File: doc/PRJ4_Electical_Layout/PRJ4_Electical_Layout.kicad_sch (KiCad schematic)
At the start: 10 parts, among them M1 Motor_DC, M2 Motor_DC, U5 MCP23017_SO

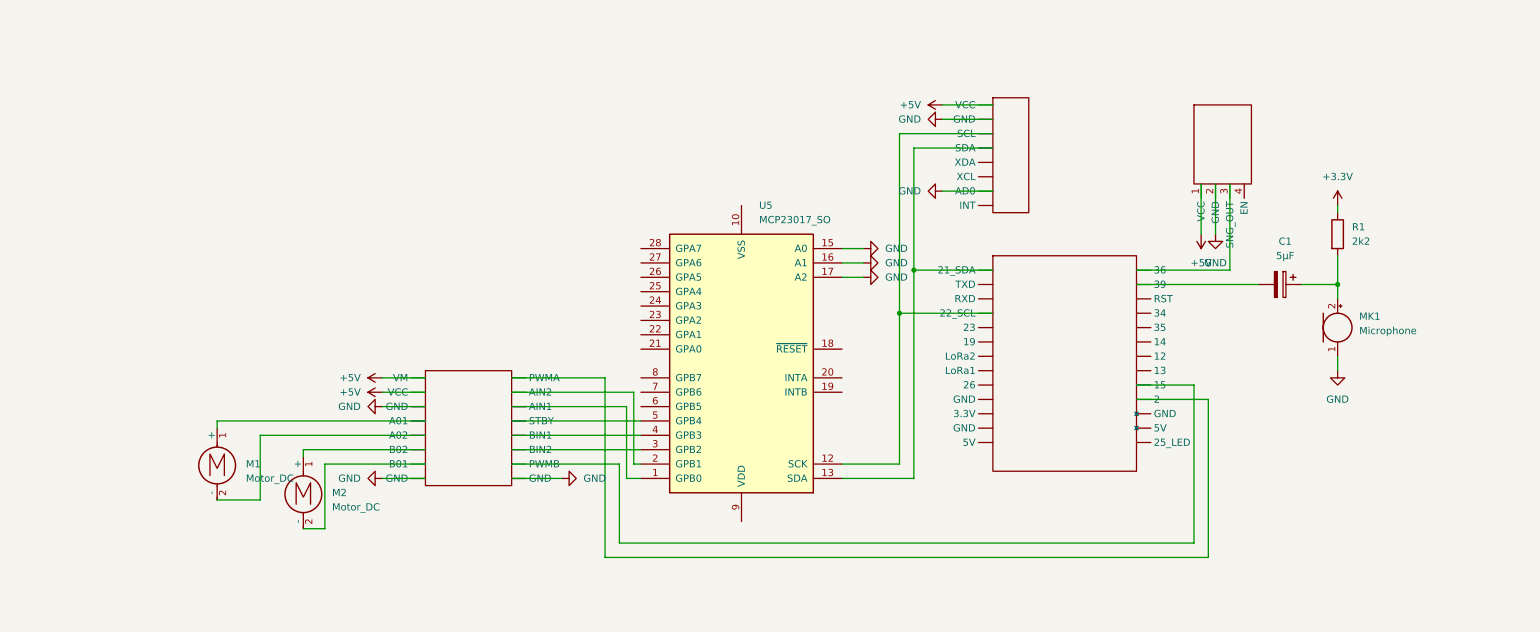
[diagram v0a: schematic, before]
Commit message: Add new components
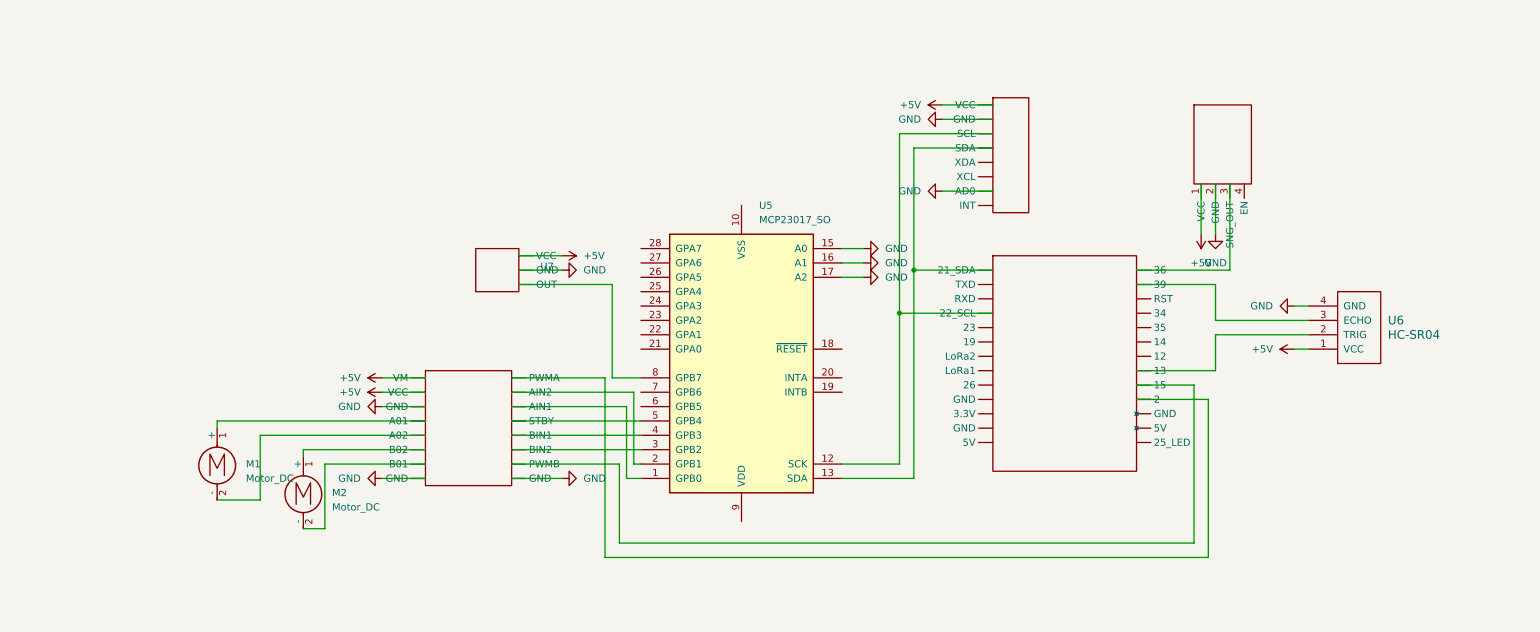
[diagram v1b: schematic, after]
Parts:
- removed C1: 5µF, symbol Device:C_Polarized
- removed MK1: Microphone, symbol Device:Microphone
- removed R1: 2k2, symbol Device:R
- added U6: HC-SR04, symbol hc-sr04:HC-SR04
- added U7: ~, symbol prj4:MAX4466
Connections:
- net +5V: now also U6.1 (VCC), U7. (VCC)
- net GND: now also U6.4 (GND), U7. (VCC)
- net at U2. (25_LED): now also U6.3 (ECHO)
- net at U5.8 (GPB7): now also U7. (VCC)
- new net: U2. (25_LED), U3. (INT), U5.12 (SCK)
- new net: U2. (25_LED), U3. (INT), U5.13 (SDA)
- new net: U2. (25_LED), U4. (GND) (x2)
- new net: U2. (25_LED), U6.2 (TRIG)

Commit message: Update layout with new 2. mic
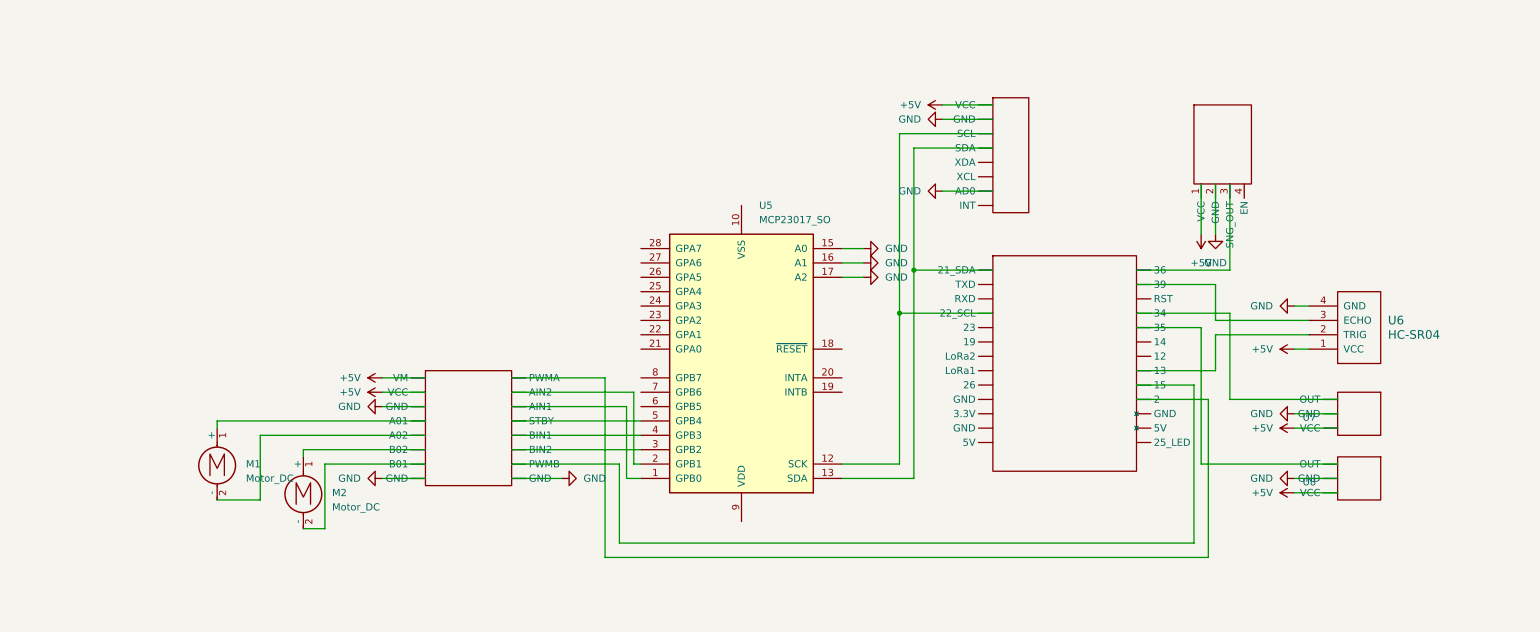
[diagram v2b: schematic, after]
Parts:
- added U8: ~, symbol prj4:MAX4466
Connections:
- net +5V: now also U8. (VCC)
- net GND: now also U8. (VCC)
- net at U2. (25_LED): now also U6.3 (ECHO)
- net at U5.8 (GPB7): no longer U7. (VCC)
- new net: U2. (25_LED), U3. (INT), U5.12 (SCK)
- new net: U2. (25_LED), U3. (INT), U5.13 (SDA)
- new net: U2. (25_LED), U7. (VCC)
- new net: U2. (25_LED), U8. (VCC)
- new net: U2. (25_LED), U4. (GND) (x2)
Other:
- moved on the sheet: U7

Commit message: add new components plus change esp 32
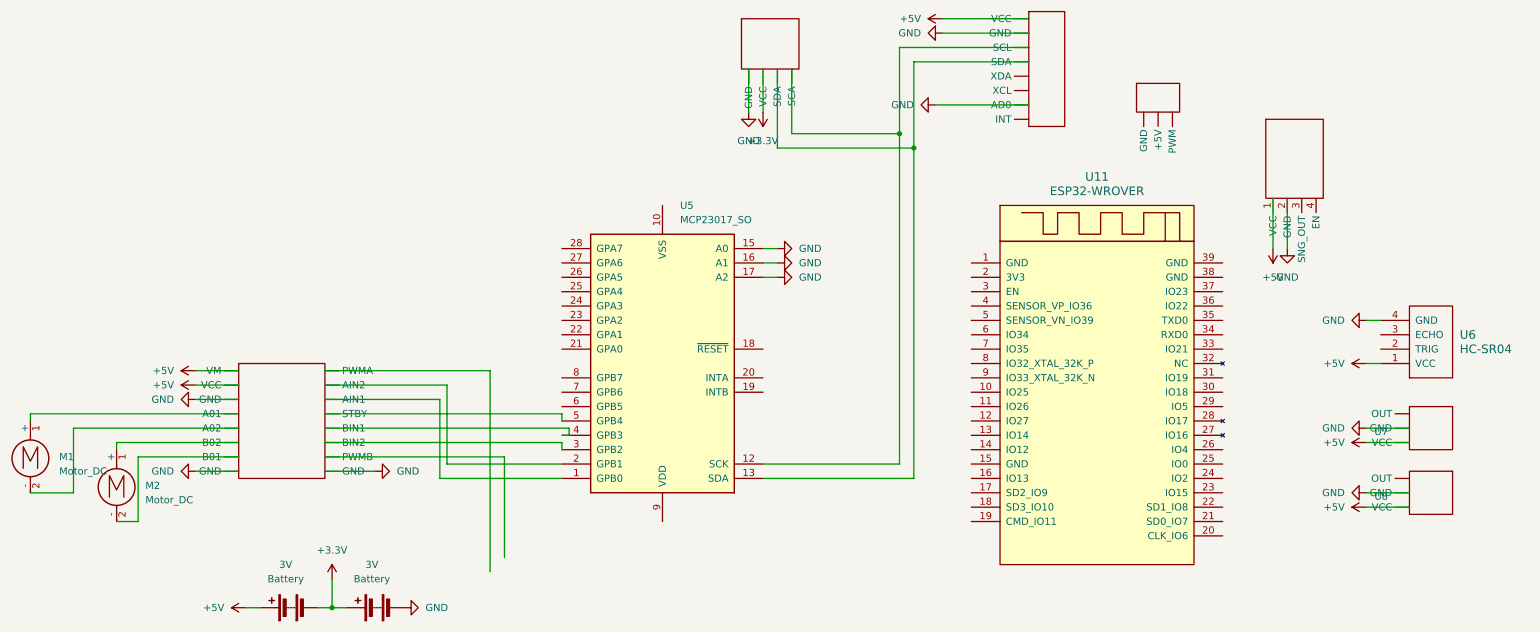
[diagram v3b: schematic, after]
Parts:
- removed U2: ~, symbol prj4:lilygo_t3
- added 3V (x2): Battery, symbol Device:Battery
- added U10: ~, symbol prj4:996_Servo
- added U11: ESP32-WROVER, symbol esp32-wrover:ESP32-WROVER
- added U9: ~, symbol prj4:Monitor
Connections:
- net +5V: now also 3V.1 (+)
- net GND: now also 3V.2 (-), U9. (SCA)
- net at U3. (INT), U5.12 (SCK): now also U9. (SCA)
- net at U3. (INT), U5.13 (SDA): now also U9. (SCA)
- new net +3.3V: 3V.1 (+), 3V.2 (-), U9. (SCA)
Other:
- moved on the sheet: M1, M2, U5, U6, U7, U8

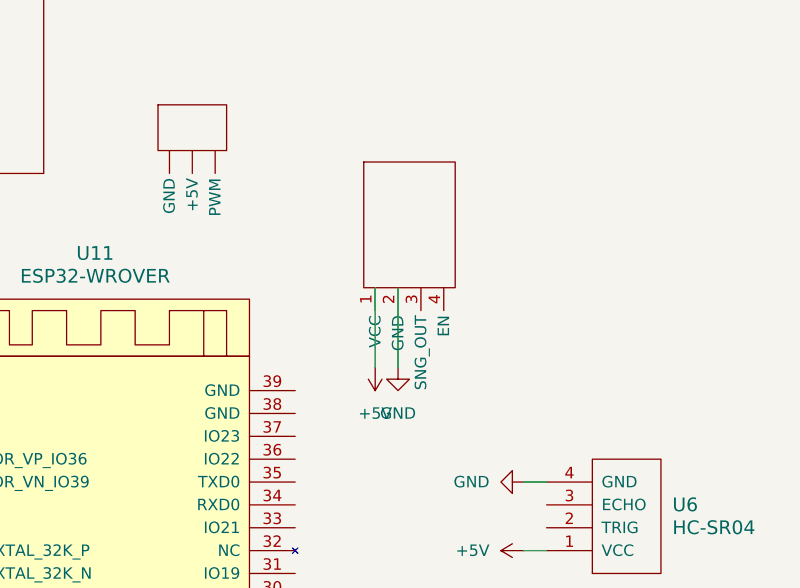
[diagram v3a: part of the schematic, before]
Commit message: remove ir sensor
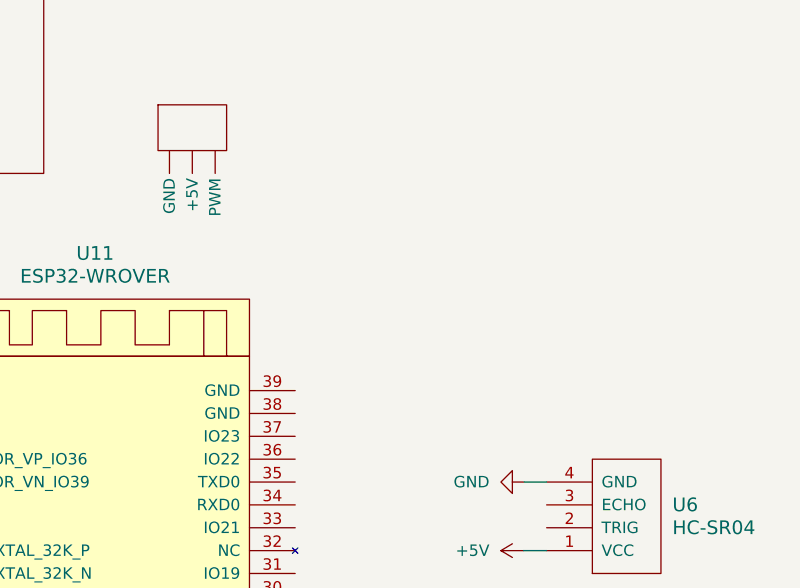
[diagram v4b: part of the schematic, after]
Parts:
- removed U1: ~, symbol prj4:SEN-KY032IR
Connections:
- new net: U3. (INT), U5.12 (SCK), U9. (SCA)
- new net: U3. (INT), U5.13 (SDA), U9. (SCA)
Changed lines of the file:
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@@
 	(wire
 		(pts
-			(xy 243.84 57.15) (xy 243.84 66.04)
+			(xy 50.8 105.41) (xy 58.42 105.41)
 		)
 		(stroke
@@
 	(wire
 		(pts
-			(xy 50.8 105.41) (xy 58.42 105.41)
+			(xy 21.59 95.25) (xy 21.59 96.52)
 		)
 		(stroke
@@
 	(wire
 		(pts
-			(xy 21.59 95.25) (xy 21.59 96.52)
+			(xy 151.13 66.04) (xy 153.67 66.04)
 		)
 		(stroke
@@
 	(wire
 		(pts
-			(xy 151.13 66.04) (xy 153.67 66.04)
+			(xy 151.13 104.14) (xy 175.26 104.14)
 		)
 		(stroke
@@
 	(wire
 		(pts
-			(xy 151.13 104.14) (xy 175.26 104.14)
+			(xy 58.42 100.33) (xy 36.83 100.33)
 		)
 		(stroke
@@
 	(wire
 		(pts
-			(xy 58.42 100.33) (xy 36.83 100.33)
+			(xy 177.8 33.02) (xy 198.12 33.02)
 		)
 		(stroke
@@
 	(wire
 		(pts
-			(xy 177.8 33.02) (xy 198.12 33.02)
+			(xy 29.21 109.22) (xy 21.59 109.22)
 		)
 		(stroke
@@
 	(wire
 		(pts
-			(xy 29.21 109.22) (xy 21.59 109.22)
+			(xy 74.93 124.46) (xy 74.93 129.54)
 		)
 		(stroke
@@
 	(wire
 		(pts
-			(xy 74.93 124.46) (xy 74.93 129.54)
+			(xy 74.93 129.54) (xy 77.47 129.54)
 		)
 		(stroke
@@
 	(wire
 		(pts
-			(xy 74.93 129.54) (xy 77.47 129.54)
+			(xy 73.66 90.17) (xy 95.25 90.17)
 		)
 		(stroke
@@
 	(wire
 		(pts
-			(xy 73.66 90.17) (xy 95.25 90.17)
+			(xy 148.59 34.29) (xy 148.59 41.91)
 		)
 		(stroke
@@
 	(wire
 		(pts
-			(xy 148.59 34.29) (xy 148.59 41.91)
+			(xy 50.8 90.17) (xy 58.42 90.17)
 		)
 		(stroke
@@
 	(wire
 		(pts
-			(xy 50.8 90.17) (xy 58.42 90.17)
+			(xy 177.8 33.02) (xy 177.8 48.26)
 		)
 		(stroke
@@
 	(wire
 		(pts
-			(xy 177.8 33.02) (xy 177.8 48.26)
+			(xy 177.8 48.26) (xy 177.8 106.68)
 		)
 		(stroke
@@
 	(wire
 		(pts
-			(xy 177.8 48.26) (xy 177.8 106.68)
+			(xy 198.12 30.48) (xy 175.26 30.48)
 		)
 		(stroke
@@
 	(wire
 		(pts
-			(xy 198.12 30.48) (xy 175.26 30.48)
+			(xy 156.21 45.72) (xy 175.26 45.72)
 		)
 		(stroke
@@
 	(wire
 		(pts
-			(xy 156.21 45.72) (xy 175.26 45.72)
+			(xy 93.98 106.68) (xy 115.57 106.68)
 		)
 		(stroke
@@
 	(wire
 		(pts
-			(xy 241.3 57.15) (xy 241.3 66.04)
+			(xy 73.66 87.63) (xy 102.87 87.63)
 		)
 		(stroke
@@
 	(wire
 		(pts
-			(xy 93.98 106.68) (xy 115.57 106.68)
+			(xy 156.21 34.29) (xy 156.21 45.72)
 		)
 		(stroke
@@
 	(wire
 		(pts
-			(xy 73.66 87.63) (xy 102.87 87.63)
+			(xy 58.42 97.79) (xy 29.21 97.79)
 		)
 		(stroke
@@
 		)
 	)
-	(wire
-		(pts
-			(xy 156.21 34.29) (xy 156.21 45.72)
-		)
-		(stroke
-			(width 0)
-			(type default)
-		)
-	)
-	(wire
-		(pts
-			(xy 58.42 97.79) (xy 29.21 97.79)
-		)
-		(stroke
-			(width 0)
-			(type default)
-		)
-	)
 	(symbol
 		(lib_id "power:+5V")
@@
 				(path "/cdbfb8fb-cebf-44e8-ba3a-bda7c53d363b"
 					(reference "#PWR019")
-					(unit 1)
-				)
-			)
-		)
-	)
-	(symbol
-		(lib_id "prj4:SEN-KY032IR")
-		(at 245.11 49.53 0)
-		(unit 1)
-		(exclude_from_sim no)
-		(in_bom yes)
-		(on_board yes)
-		(dnp no)
-		(fields_autoplaced yes)
-		(property "Reference" "U1"
-			(at 245.11 49.53 0)
-			(effects
-				(font
-					(size 1.27 1.27)
-				)
-				(hide yes)
-			)
-		)
-		(property "Value" "~"
-			(at 251.46 51.435 0)
-			(effects
-				(font
-					(size 1.27 1.27)
-				)
-				(justify left)
-			)
-		)
-		(property "Footprint" ""
-			(at 245.11 49.53 0)
-			(effects
-				(font
-					(size 1.27 1.27)
-				)
-				(hide yes)
-			)
-		)
-		(property "Datasheet" ""
-			(at 245.11 49.53 0)
-			(effects
-				(font
-					(size 1.27 1.27)
-				)
-				(hide yes)
-			)
-		)
-		(property "Description" ""
-			(at 245.11 49.53 0)
-			(effects
-				(font
-					(size 1.27 1.27)
-				)
-				(hide yes)
-			)
-		)
-		(pin "3"
-		)
-		(pin "2"
-		)
-		(pin "4"
-		)
-		(pin "1"
-		)
-		(instances
-			(project ""
-				(path "/cdbfb8fb-cebf-44e8-ba3a-bda7c53d363b"
-					(reference "U1")
 					(unit 1)
 				)
@@
 	)
 	(symbol
-		(lib_id "power:+5V")
-		(at 241.3 66.04 180)
-		(unit 1)
-		(exclude_from_sim no)
-		(in_bom yes)
-		(on_board yes)
-		(dnp no)
-		(fields_autoplaced yes)
-		(property "Reference" "#PWR01"
-			(at 241.3 62.23 0)
-			(effects
-				(font
-					(size 1.27 1.27)
-				)
-				(hide yes)
-			)
-		)
-		(property "Value" "+5V"
-			(at 241.3 71.12 0)
-			(effects
-				(font
-					(size 1.27 1.27)
-				)
-			)
-		)
-		(property "Footprint" ""
-			(at 241.3 66.04 0)
-			(effects
-				(font
-					(size 1.27 1.27)
-				)
-				(hide yes)
-			)
-		)
-		(property "Datasheet" ""
-			(at 241.3 66.04 0)
-			(effects
-				(font
-					(size 1.27 1.27)
-				)
-				(hide yes)
-			)
-		)
-		(property "Description" "Power symbol creates a global label with name \"+5V\""
-			(at 241.3 66.04 0)
-			(effects
-				(font
-					(size 1.27 1.27)
-				)
-				(hide yes)
-			)
-		)
-		(pin "1"
-		)
-		(instances
-			(project ""
-				(path "/cdbfb8fb-cebf-44e8-ba3a-bda7c53d363b"
-					(reference "#PWR01")
-					(unit 1)
-				)
-			)
-		)
-	)
-	(symbol
 		(lib_id "power:GND")
 		(at 257.81 97.79 270)
@@
 					(unit 1)
 				)
-			)
-		)
-	)
-	(symbol
-		(lib_id "power:GND")
-		(at 243.84 66.04 0)
-		(unit 1)
-		(exclude_from_sim no)
-		(in_bom yes)
-		(on_board yes)
-		(dnp no)
-		(fields_autoplaced yes)
-		(property "Reference" "#PWR02"
-			(at 243.84 72.39 0)
-			(effects
-				(font
-					(size 1.27 1.27)
-				)
-				(hide yes)
-			)
-		)
-		(property "Value" "GND"
-			(at 243.84 71.12 0)
-			(effects
-				(font
-					(size 1.27 1.27)
-				)
-			)
-		)
-		(property "Footprint" ""
-			(at 243.84 66.04 0)
-			(effects
-				(font
-					(size 1.27 1.27)
-				)
-				(hide yes)
-			)
-		)
-		(property "Datasheet" ""
-			(at 243.84 66.04 0)
-			(effects
-				(font
-					(size 1.27 1.27)
-				)
-				(hide yes)
-			)
-		)
-		(property "Description" "Power symbol creates a global label with name \"GND\" , ground"
-			(at 243.84 66.04 0)
-			(effects
-				(font
-					(size 1.27 1.27)
-				)
-				(hide yes)
-			)
-		)
-		(pin "1"
-		)
-		(instances
-			(project ""
-				(path "/cdbfb8fb-cebf-44e8-ba3a-bda7c53d363b"
-					(reference "#PWR02")
-					(unit 1)
-				)

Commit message: fix lable
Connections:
- net +3.3V: no longer 3V.1 (+), 3V.2 (-)
- net +5V: no longer 3V.1 (+)
- net at U11.20 (CLK_IO6): now also U11.21 (SD0_IO7), U3. (INT), U5.13 (SDA), U9. (SCA)
- net at U11.22 (SD1_IO8): now also U3. (INT), U5.12 (SCK), U9. (SCA)
- net at U11.23 (IO15): now also U8. (VCC)
- net at U11.24 (IO2): now also U4. (GND)
- net at U11.26 (IO4): now also U7. (VCC)
- net at U11.29 (IO5): now also U4. (GND)
- net at U11.30 (IO18): now also U6.2 (TRIG)
- net at U11.31 (IO19): now also U6.3 (ECHO)
- net at U11.37 (IO23): now also U10. (PWM)
- new net: 3V.1 (+), 3V.2 (-)
- new net +6V: 3V.1 (+)
